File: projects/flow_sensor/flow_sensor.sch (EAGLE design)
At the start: 85 parts, among them J5 455-1750-1-ND

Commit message: Tentative board v2.0 complete
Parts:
- removed LIPO: (no value), SparkFun-Connectors:CONN_021X02_NO_SILK
- removed R21, R22: 47, SparkFun-Resistors:680OHM-0603-1/10W-5%
- removed R23: 20, SparkFun-Resistors:680OHM-0603-1/10W-5%
- removed R35: 800, SparkFun-Resistors:787OHM-0603-1/10W-1%
- removed U$3: F552X---PN80, TI_MSP430_v16:F552X---PN80
- added C44, C49: 0.1uF, SparkFun-Capacitors:0.1UF-0603-25V-(+80/-20%)
- added C50: 470nF, SparkFun-Capacitors:0.1UF-0603-25V-(+80/-20%)
- added J4: (no value), SparkFun-Connectors:CONN_02
- added R14: 680, SparkFun-Resistors:680OHM-0603-1/10W-5%
- added R15: 20, SparkFun-Resistors:680OHM-0603-1/10W-5%
- added R16, R17: 47, SparkFun-Resistors:680OHM-0603-1/10W-5%
- added R4, R5: 10k, SparkFun-Resistors:10KOHM-0603-1/10W-1%
- added U9: F552X---PN80, my_library:F552X---PN80
- added Y2: 32.768kHz, SparkFun-Clocks:CRYSTALSMD-3.2X2.5
- added Y3: 4MHz, SparkFun-Clocks:CRYSTALSMD-3.2X2.5
- C1: value 0.1uF -> 3.3uF
- C10, C8: value 2.2uF -> 0.1uF; device SparkFun-Capacitors:2.2UF-0603-10V-20% -> SparkFun-Capacitors:0.1UF-0603-25V-(+80/-20%)
- C11: value 10nF -> 3uF; device SparkFun-Capacitors:10NF-0603-50V-10% -> SparkFun-Capacitors:4.7UF0603
- C12: value 2.2uF -> 3uF; device SparkFun-Capacitors:2.2UF-0603-10V-20% -> SparkFun-Capacitors:4.7UF0603
- C13, C9: value 10nF -> 0.1uF; device SparkFun-Capacitors:10NF-0603-50V-10% -> SparkFun-Capacitors:0.1UF-0603-25V-(+80/-20%)
- C14: value 2.2uF -> 10nF; device SparkFun-Capacitors:2.2UF-0603-10V-20% -> SparkFun-Capacitors:10NF-0603-50V-10%
- C15: value 1.5nF -> 2.2uF; device SparkFun-Capacitors:1.0NF/1000PF-0603-50V-10% -> SparkFun-Capacitors:2.2UF-0603-10V-20%
- C16: value 1.2nF -> 10nF; device SparkFun-Capacitors:1.0NF/1000PF-0603-50V-10% -> SparkFun-Capacitors:10NF-0603-50V-10%
- C17: value 1.2nF -> 2.2uF; device SparkFun-Capacitors:1.0NF/1000PF-0603-50V-10% -> SparkFun-Capacitors:2.2UF-0603-10V-20%
- C18: value 1.5nF -> 10nF; device SparkFun-Capacitors:1.0NF/1000PF-0603-50V-10% -> SparkFun-Capacitors:10NF-0603-50V-10%
- C19: value 680pF -> 2.2uF; device SparkFun-Capacitors:1.0NF/1000PF-0603-50V-10% -> SparkFun-Capacitors:2.2UF-0603-10V-20%
- C2: value 1uF -> 0.1uF; device SparkFun-Capacitors:4.7UF0603 -> SparkFun-Capacitors:0.1UF-0603-25V-(+80/-20%)
- C20: value 10pF -> 10nF; device SparkFun-Capacitors:10PF-0603-50V-5% -> SparkFun-Capacitors:10NF-0603-50V-10%
- C21: value 680pF -> 2.2uF; device SparkFun-Capacitors:680PF-0603-50V-10% -> SparkFun-Capacitors:2.2UF-0603-10V-20%
- C22: value 220pF -> 10nF; device SparkFun-Capacitors:270PF-0603-50V-5% -> SparkFun-Capacitors:10NF-0603-50V-10%
- C23: value 100pF -> 2.2uF; device SparkFun-Capacitors:100PF-0603-50V-5% -> SparkFun-Capacitors:2.2UF-0603-10V-20%
- C25: value 1.0uF -> 1.5nF; device SparkFun-Capacitors:1.0UF-0603-16V-10% -> SparkFun-Capacitors:1.0NF/1000PF-0603-50V-10%
- C26: value 0.1uF -> 1.5nF; device SparkFun-Capacitors:0.1UF-0603-25V-(+80/-20%) -> SparkFun-Capacitors:1.0NF/1000PF-0603-50V-10%
- C27: value 3.3uF -> 27pF; device SparkFun-Capacitors:0.1UF-0603-25V-(+80/-20%) -> SparkFun-Capacitors:27PF-0603-50V-5%
- C28: value 3uF -> 1.2nF; device SparkFun-Capacitors:4.7UF0603 -> SparkFun-Capacitors:1.0NF/1000PF-0603-50V-10%
- C29: value 1uF -> 1.2nF; device SparkFun-Capacitors:0.1UF-0603-25V-(+80/-20%) -> SparkFun-Capacitors:1.0NF/1000PF-0603-50V-10%
- C3: value 27pF -> 10uF; device SparkFun-Capacitors:27PF-0603-50V-5% -> SparkFun-Capacitors:0.1UF-0603-25V-(+80/-20%)
- C30: value 2.2n -> 680pF; device SparkFun-Capacitors:1.0UF-0603-16V-10% -> SparkFun-Capacitors:1.0NF/1000PF-0603-50V-10%
- C31: value 1.0uF -> 10pF; device SparkFun-Capacitors:1.0UF-0603-16V-10% -> SparkFun-Capacitors:10PF-0603-50V-5%
- C32: value 0.1uF -> 220pF; device SparkFun-Capacitors:0.1UF-0603-25V-(+80/-20%) -> SparkFun-Capacitors:270PF-0603-50V-5%
- C33: value 0.1uF -> 680pF; device SparkFun-Capacitors:0.1UF-0603-25V-(+80/-20%) -> SparkFun-Capacitors:680PF-0603-50V-10%
- C34: value 68.0pF -> 100pF; device SparkFun-Capacitors:1.0PF-0603-50V-25% -> SparkFun-Capacitors:100PF-0603-50V-5%
- C35: value 1.0pF -> 27pF; device SparkFun-Capacitors:1.0PF-0603-50V-25% -> SparkFun-Capacitors:27PF-0603-50V-5%
- C36: value 68.0pF -> 50pF; device SparkFun-Capacitors:1.0PF-0603-50V-25% -> my_library:TZY2_TRIM_CAP
- C37, C38: value 0.1uF -> 68pF; device SparkFun-Capacitors:0.1UF-0603-25V-(+80/-20%) -> capacitor-wima:C2.5/2
- C39: value 0.1uF -> 50pF; device SparkFun-Capacitors:0.1UF-0603-25V-(+80/-20%) -> my_library:TZY2_TRIM_CAP
- C4: value 27pF -> 1uF; device SparkFun-Capacitors:27PF-0603-50V-5% -> SparkFun-Capacitors:4.7UF0603
- C40: value 10uF -> 1uF
- C41: value 3uF -> 1.0uF; device SparkFun-Capacitors:4.7UF0603 -> SparkFun-Capacitors:1.0UF-0603-16V-10%
- C42: value 1.0pF -> 0.1uF; device SparkFun-Capacitors:1.0PF-0603-50V-25% -> SparkFun-Capacitors:0.1UF-0603-25V-(+80/-20%)
- C43: value 0.1uF -> 1.0uF; device SparkFun-Capacitors:0.1UF-0603-25V-(+80/-20%) -> SparkFun-Capacitors:1.0UF-0603-16V-10%
- C45: value 1uF -> 2.2n; device SparkFun-Capacitors:4.7UF0603 -> SparkFun-Capacitors:1.0UF-0603-16V-10%
- C46, C47: value 1uF -> 47pF; device SparkFun-Capacitors:4.7UF0603 -> SparkFun-Capacitors:0.1UF-0603-25V-(+80/-20%)
- C5, C7: value 10nF -> 1uF; device SparkFun-Capacitors:10NF-0603-50V-10% -> SparkFun-Capacitors:4.7UF0603
- C6: value 2.2uF -> 1uF; device SparkFun-Capacitors:2.2UF-0603-10V-20% -> SparkFun-Capacitors:4.7UF0603
- J1: value (none) -> 1X07_CONNECTOR; device SparkFun-Connectors:CONN_02 -> my_library:1X07_CONNECTOR
- J2: value (none) -> 1X03_CONNECTOR; device SparkFun-Connectors:CONN_02 -> my_library:1X03_CONNECTOR
- J3: device SparkFun-Connectors:CONN_07 -> SparkFun-Connectors:CONN_021X02_NO_SILK
- J5: value 455-1750-1-ND -> (none); device SparkFun-Connectors:CONN_03 -> SparkFun-Connectors:CONN_02
- R1: value 47k -> 56k; device SparkFun-Resistors:680OHM-0603-1/10W-5% -> SparkFun-Resistors:20KOHM-0603-1/10W-1%
- R10: value 600 -> 1k; device SparkFun-Resistors:787OHM-0603-1/10W-1% -> my_library:PVG3G_TRIM_POT
- R12: value 27k -> 10k; device SparkFun-Resistors:20KOHM-0603-1/10W-1% -> SparkFun-Resistors:10KOHM-0603-1/10W-1%
- R13: value 56k -> 10k; device SparkFun-Resistors:20KOHM-0603-1/10W-1% -> SparkFun-Resistors:10KOHM-0603-1/10W-1%
- R18: value 680 -> 47k
- R19, R20: value 10k -> 50; device SparkFun-Resistors:10KOHM-0603-1/10W-1% -> my_library:PVG3G_TRIM_POT
- R2: value 10k -> 27k; device SparkFun-Resistors:10KOHM-0603-1/10W-1% -> SparkFun-Resistors:20KOHM-0603-1/10W-1%
- R9: value 10k -> 1k; device SparkFun-Resistors:10KOHM-0603-1/10W-1% -> my_library:PVG3G_TRIM_POT
- Y1: value (none) -> 13.56MHz
- renumbered U$1 to U3, U$10 to U8, U$2 to U7, U$4 to U5, U$5 to U6, U$6 to U4, U$7 to U2, U$8 to U1
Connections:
- removed net 3.3V: R11.1, R7.1
- removed net N$31: D3.A, R23.1
- removed net N$37: R35.1, U5.RG1
- removed net N$40: R35.2, U5.RG1'
- new net N$17: D3.A, U9.77
- new net N$20: C36.P$2, C37.2, C38.1, C39.P$2, R14.1
- new net N$22: R9.2, U5.RG1
- new net N$25: C36.P$1, C37.1, J4.2
- new net N$28: C47.1, U9.69, Y3.2
- new net N$30: C46.1, U9.70, Y3.1
- new net N$35: R20.1, R4.1
- new net N$5: D1.A, U9.79
- new net N$7: D2.A, U9.78
- new net XIN: U9.12, Y2.1
- new net XOUT: U9.13, Y2.2
- net 3V3: now also J1.5; no longer J3.3
- net 5V: now also J1.6, J2.2; no longer J3.2, J5.2
- net ANT: now also C31.2, C32.1, C34.1, C35.1, J4.1; no longer C20.2, C22.1, C23.1, C24.1, J1.1
- net BRIDGE_VCC: now also R5.2, U9.42; no longer R6.2
- net CHG_STAT: now also R1.2, U9.53; no longer R13.2
- net COMMS_EN: now also R13.1, U9.44; no longer R2.1
- net COMMS_IRQ: now also U9.21
- net COMMS_SS: now also U9.60
- net GND: now also C1.2, C10.1, C13.1, C15.2, C16.2, C18.2, C19.2, C20.2, C22.2, C27.1, C33.2, C38.2, C39.P$1, C41.1, C43.1, C44.1, C46.2, C47.2, C49.1, C5.1, C50.1, C6.1, C7.1, C9.1, J1.7, J3.2, J5.1, J5.2, R13.2, R14.2, R15.1, R16.1, R17.1, R19.2, R2.1, R20.2, U9.14, U9.19, U9.49, U9.61, U9.68; no longer C1.1, C10.2, C12.2, C13.2, C19.1, C2.1, C25.1, C26.1, C27.2, C28.2, C31.1, C32.1, C33.1, C36.1, C36.2, C38.1, C39.1, C42.2, C43.2, C46.1, C47.1, C5.2, C6.2, C7.2, C9.2, D1.C, D2.C, D3.C, J2.1, J2.2, J3.1, LIPO.2, R12.1, R18.1, R18.2, R2.2, U$3.14, U$3.19, U$3.49, U$3.68, U7.TH_PAD
- net MEM_SS: now also U9.55
- net MISO: now also U9.47
- net MOSI: now also U9.46
- net N$1: now also D2.C, R16.2; no longer R22.2
- net N$10: now also C27.2; no longer C4.2
- net N$11: now also C22.1, C23.1; no longer C13.1, C14.1
- net N$12: now also C25.2, C26.1; no longer C15.1, C18.2
- net N$13: now also C28.1, C30.2, C31.1; no longer C16.1, C19.2, C20.1
- net N$14: now also C28.2, C29.1; no longer C16.2, C17.1
- net N$15: now also C25.1, C26.2; no longer C15.2, C18.1
- net N$16: now also C32.2, C33.1; no longer C21.1, C22.2
- net N$18: now also R5.1, R6.2; no longer R6.1, R7.2
- net N$19: now also C11.1, R12.2; no longer C28.1, R9.2
- net N$2: now also C2.1; no longer C37.1
- net N$21: now also C12.1; no longer C41.1
- net N$26: now also R8.2; no longer R20.2
- net N$27: now also R9.1, U5.RG1'; no longer C34.1, C35.1, J1.2
- net N$29: now also R4.2; no longer R11.2
- net N$3: now also C2.2; no longer C37.2
- net N$32: now also C50.2, U9.20; no longer D2.A, R22.1
- net N$33: now also R19.1, R6.1; no longer D1.A, R21.1
- net N$34: now also D3.C, R17.2; no longer R21.2
- net N$36: now also C12.2, R11.2, R12.1; no longer C41.2, R8.2, R9.1
- net N$38: now also D1.C, R15.2; no longer R23.2
- net N$39: now also R2.2; no longer R12.2
- net N$4: now also C24.1; no longer C3.1
- net N$43: now also R11.1; no longer R8.1
- net N$6: now also R7.2; no longer R19.2
- net N$8: now also C18.1, C19.1; no longer C10.1, C9.1
- net N$9: now also C20.1, C21.1; no longer C11.1, C12.1
- net RXD: now also J1.4, U9.41; no longer J3.4, U$3.41
- net SBWTCK: now also J1.1, U9.71; no longer J3.7, U$3.71
- net SBWTDIO: now also C45.2, J1.2, R18.1, U9.76; no longer C30.2, J3.6, R1.1, U$3.76
- net SCK: now also U9.48
- net SENSOR_OUT: now also U9.80
- net TEMP_SS: now also U9.43
- net TXD: now also J1.3, U9.40; no longer J3.5, U$3.40
- net VBAT: now also C5.2, C6.2, J2.1, J3.1, U9.1; no longer C2.2, C45.2, J5.1, LIPO.1
- net VCC: now also C10.2, C13.2, C14.1, C15.1, C40.1, C41.2, C42.2, C43.2, C44.2, C49.2, C7.2, C8.1, C9.2, R18.2, R7.1, R8.1, U9.11, U9.18, U9.50; no longer C1.2, C25.2, C26.2, C29.1, C31.2, C32.2, C33.2, C38.2, C39.2, C43.1, C47.2, C5.1, C6.1, R1.2, R19.1, R20.1, U$3.11, U$3.18, U$3.50
- net VCHGR: now also C3.1, C4.2, J2.3, R1.1; no longer C40.1, C46.2, J5.3, R13.1
- net VIN: now also C1.1, C16.1, C17.1; no longer C27.1, C7.1, C8.1

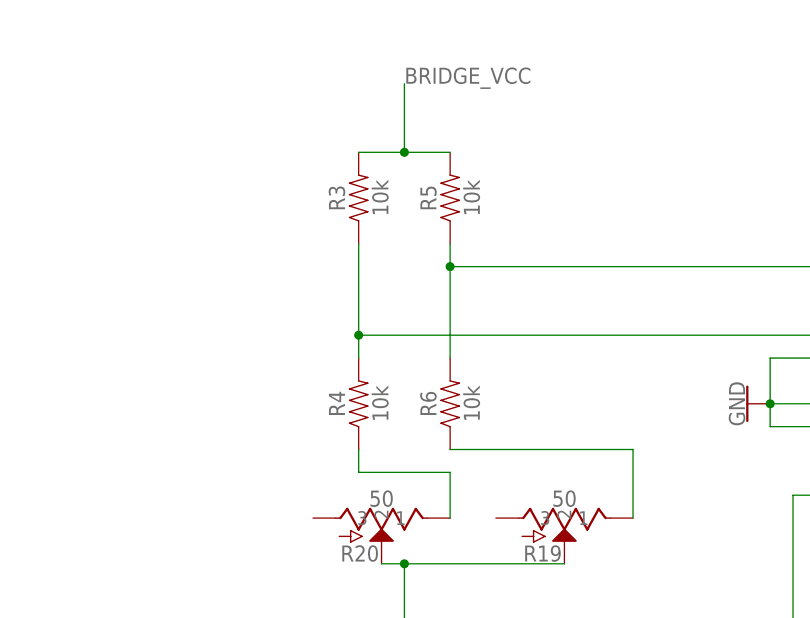
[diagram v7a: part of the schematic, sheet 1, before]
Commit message: Replaced 32k and 4M oscillator packages, added magnetic sensors, minor rewiring; board 2 almost ready for order
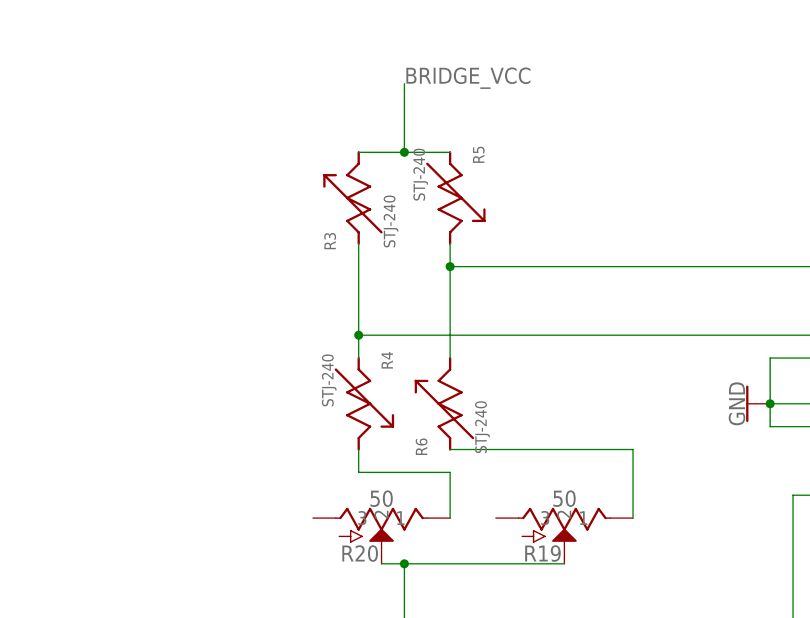
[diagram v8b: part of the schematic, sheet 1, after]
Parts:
- R3, R4, R5, R6: value 10k -> STJ-240; device SparkFun-Resistors:10KOHM-0603-1/10W-1% -> my_library:STJ-240
- Y2, Y3: device SparkFun-Clocks:CRYSTALSMD-3.2X2.5 -> my_library:CRYSTAL-3.2X1.5
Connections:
- net BRIDGE_VCC: now also R3.P$2, R5.P$1; no longer R3.2, R5.2
- net N$18: now also R3.P$1, R4.P$1, U5.+IN1; no longer R5.1, R6.2, U5.-IN1
- net N$29: now also R5.P$2, R6.P$2, U5.-IN1; no longer R3.1, R4.2, U5.+IN1
- net N$33: now also R6.P$1; no longer R6.1
- net N$35: now also R4.P$2; no longer R4.1
- net XIN: now also Y2.2; no longer Y2.1
- net XOUT: now also Y2.1; no longer Y2.2
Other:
- moved on the sheet: R3, R4, R5, R6, Y2
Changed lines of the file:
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@@
 <part name="C44" library="SparkFun-Capacitors" deviceset="0.1UF" device="-0603-25V-(+80/-20%)" value="0.1uF"/>
 <part name="GND37" library="SparkFun-PowerSymbols" deviceset="GND" device=""/>
-<part name="R5" library="SparkFun-Resistors" deviceset="10KOHM" device="-0603-1/10W-1%" value="10k"/>
-<part name="R3" library="SparkFun-Resistors" deviceset="10KOHM" device="-0603-1/10W-1%" value="10k"/>
-<part name="R4" library="SparkFun-Resistors" deviceset="10KOHM" device="-0603-1/10W-1%" value="10k"/>
-<part name="R6" library="SparkFun-Resistors" deviceset="10KOHM" device="-0603-1/10W-1%" value="10k"/>
 <part name="C1" library="SparkFun-Capacitors" deviceset="0.1UF" device="-0603-25V-(+80/-20%)" value="3.3uF"/>
 <part name="C16" library="SparkFun-Capacitors" deviceset="10NF" device="-0603-50V-10%" value="10nF"/>
@@
 <part name="R9" library="my_library" deviceset="PVG3G_TRIM_POT" device="" value="1k"/>
 <part name="R10" library="my_library" deviceset="PVG3G_TRIM_POT" device="" value="1k"/>
-<part name="Y2" library="SparkFun-Clocks" deviceset="CRYSTAL" device="SMD-3.2X2.5" value="32.768kHz"/>
-<part name="Y3" library="SparkFun-Clocks" deviceset="CRYSTAL" device="SMD-3.2X2.5" value="4MHz"/>
+<part name="Y3" library="my_library" deviceset="CRYSTAL-3.2X1.5" device="" value="4MHz"/>
 <part name="C47" library="SparkFun-Capacitors" deviceset="0.1UF" device="-0603-25V-(+80/-20%)" value="47pF"/>
 <part name="C46" library="SparkFun-Capacitors" deviceset="0.1UF" device="-0603-25V-(+80/-20%)" value="47pF"/>
@@
 <part name="C50" library="SparkFun-Capacitors" deviceset="0.1UF" device="-0603-25V-(+80/-20%)" value="470nF"/>
 <part name="GND44" library="SparkFun-PowerSymbols" deviceset="GND" device=""/>
+<part name="R3" library="my_library" deviceset="STJ-240" device=""/>
+<part name="R4" library="my_library" deviceset="STJ-240" device=""/>
+<part name="R5" library="my_library" deviceset="STJ-240" device=""/>
+<part name="R6" library="my_library" deviceset="STJ-240" device=""/>
+<part name="Y2" library="my_library" deviceset="CRYSTAL-3.2X1.5" device="" value="32.768kHz"/>
 </parts>
 <sheets>
@@
 <instance part="GND1" gate="1" x="-73.66" y="20.32"/>
 <instance part="C2" gate="G$1" x="-73.66" y="73.66" rot="R90"/>
-<instance part="R5" gate="G$1" x="162.56" y="63.5" rot="R90"/>
-<instance part="R3" gate="G$1" x="152.4" y="63.5" rot="R90"/>
-<instance part="R4" gate="G$1" x="152.4" y="40.64" rot="R90"/>
-<instance part="R6" gate="G$1" x="162.56" y="40.64" rot="R90"/>
 <instance part="C1" gate="G$1" x="-81.28" y="33.02"/>
 <instance part="C3" gate="G$1" x="-66.04" y="33.02"/>
@@
 <instance part="R19" gate="G$1" x="175.26" y="27.94" rot="R270"/>
 <instance part="R20" gate="G$1" x="154.94" y="27.94" rot="R270"/>
+<instance part="R3" gate="G$1" x="152.4" y="63.5" rot="R90"/>
+<instance part="R4" gate="G$1" x="152.4" y="40.64" rot="R270"/>
+<instance part="R5" gate="G$1" x="162.56" y="63.5" rot="R270"/>
+<instance part="R6" gate="G$1" x="162.56" y="40.64" rot="R90"/>
 </instances>
 <busses>
@@
 <net name="N$18" class="0">
 <segment>
-<wire x1="205.74" y1="55.88" x2="162.56" y2="55.88" width="0.1524" layer="91"/>
-<pinref part="U5" gate="G$1" pin="-IN1"/>
-<pinref part="R6" gate="G$1" pin="2"/>
-<wire x1="162.56" y1="45.72" x2="162.56" y2="55.88" width="0.1524" layer="91"/>
-<pinref part="R5" gate="G$1" pin="1"/>
-<wire x1="162.56" y1="55.88" x2="162.56" y2="58.42" width="0.1524" layer="91"/>
-<junction x="162.56" y="55.88"/>
+<pinref part="U5" gate="G$1" pin="+IN1"/>
+<pinref part="R4" gate="G$1" pin="P$1"/>
+<pinref part="R3" gate="G$1" pin="P$1"/>
+<wire x1="152.4" y1="58.42" x2="152.4" y2="48.26" width="0.1524" layer="91"/>
+<wire x1="152.4" y1="48.26" x2="152.4" y2="45.72" width="0.1524" layer="91"/>
+<wire x1="205.74" y1="48.26" x2="152.4" y2="48.26" width="0.1524" layer="91"/>
+<junction x="152.4" y="48.26"/>
 </segment>
 </net>
@@
 <wire x1="157.48" y1="68.58" x2="157.48" y2="76.2" width="0.1524" layer="91"/>
 <label x="157.48" y="76.2" size="1.778" layer="95"/>
-<pinref part="R5" gate="G$1" pin="2"/>
 <wire x1="162.56" y1="68.58" x2="157.48" y2="68.58" width="0.1524" layer="91"/>
-<pinref part="R3" gate="G$1" pin="2"/>
 <wire x1="157.48" y1="68.58" x2="152.4" y2="68.58" width="0.1524" layer="91"/>
 <junction x="157.48" y="68.58"/>
+<pinref part="R3" gate="G$1" pin="P$2"/>
+<pinref part="R5" gate="G$1" pin="P$1"/>
 </segment>
 </net>
@@
 <net name="N$29" class="0">
 <segment>
-<pinref part="R3" gate="G$1" pin="1"/>
-<pinref part="R4" gate="G$1" pin="2"/>
-<wire x1="152.4" y1="58.42" x2="152.4" y2="48.26" width="0.1524" layer="91"/>
-<pinref part="U5" gate="G$1" pin="+IN1"/>
-<wire x1="152.4" y1="48.26" x2="152.4" y2="45.72" width="0.1524" layer="91"/>
-<wire x1="205.74" y1="48.26" x2="152.4" y2="48.26" width="0.1524" layer="91"/>
-<junction x="152.4" y="48.26"/>
+<pinref part="U5" gate="G$1" pin="-IN1"/>
+<wire x1="205.74" y1="55.88" x2="162.56" y2="55.88" width="0.1524" layer="91"/>
+<pinref part="R5" gate="G$1" pin="P$2"/>
+<pinref part="R6" gate="G$1" pin="P$2"/>
+<wire x1="162.56" y1="45.72" x2="162.56" y2="55.88" width="0.1524" layer="91"/>
+<wire x1="162.56" y1="55.88" x2="162.56" y2="58.42" width="0.1524" layer="91"/>
+<junction x="162.56" y="55.88"/>
 </segment>
 </net>
@@
 <segment>
 <pinref part="R19" gate="G$1" pin="1"/>
-<pinref part="R6" gate="G$1" pin="1"/>
 <wire x1="182.88" y1="27.94" x2="182.88" y2="35.56" width="0.1524" layer="91"/>
 <wire x1="182.88" y1="35.56" x2="162.56" y2="35.56" width="0.1524" layer="91"/>
+<pinref part="R6" gate="G$1" pin="P$1"/>
 </segment>
 </net>
@@
 <wire x1="162.56" y1="27.94" x2="162.56" y2="33.02" width="0.1524" layer="91"/>
 <wire x1="162.56" y1="33.02" x2="152.4" y2="33.02" width="0.1524" layer="91"/>
-<pinref part="R4" gate="G$1" pin="1"/>
 <wire x1="152.4" y1="33.02" x2="152.4" y2="35.56" width="0.1524" layer="91"/>
+<pinref part="R4" gate="G$1" pin="P$2"/>
 </segment>
 </net>
@@
 <instance part="C39" gate="G$1" x="101.6" y="22.86" rot="R90"/>
 <instance part="C36" gate="G$1" x="68.58" y="38.1"/>
-<instance part="Y2" gate="G$1" x="284.48" y="7.62" rot="R270"/>
 <instance part="Y3" gate="G$1" x="342.9" y="66.04"/>
 <instance part="C47" gate="G$1" x="350.52" y="76.2" rot="R180"/>
@@
 <instance part="C50" gate="G$1" x="299.72" y="-38.1" rot="R180"/>
 <instance part="GND44" gate="1" x="299.72" y="-50.8"/>
+<instance part="Y2" gate="G$1" x="284.48" y="7.62" rot="R90"/>
 </instances>
 <busses>
@@
 <net name="XIN" class="0">
 <segment>
-<pinref part="Y2" gate="G$1" pin="1"/>
 <wire x1="284.48" y1="10.16" x2="292.1" y2="10.16" width="0.1524" layer="91"/>
 <label x="292.1" y="10.16" size="1.778" layer="95"/>
+<pinref part="Y2" gate="G$1" pin="2"/>
 </segment>
 <segment>
@@
 <net name="XOUT" class="0">
 <segment>
-<pinref part="Y2" gate="G$1" pin="2"/>
 <wire x1="284.48" y1="5.08" x2="292.1" y2="5.08" width="0.1524" layer="91"/>
 <label x="292.1" y="5.08" size="1.778" layer="95"/>
-</segment>
-<segment>
+<pinref part="Y2" gate="G$1" pin="1"/>
+</segment>
+<segment>
